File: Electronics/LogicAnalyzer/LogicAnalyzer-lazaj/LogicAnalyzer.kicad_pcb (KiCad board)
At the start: 4 copper layers, 57 x 55.2 mm, 58 parts, among them J1 Conn_02x15_Odd_Even, J2 Conn_01x03, J3 Conn_01x03, U1 Pico

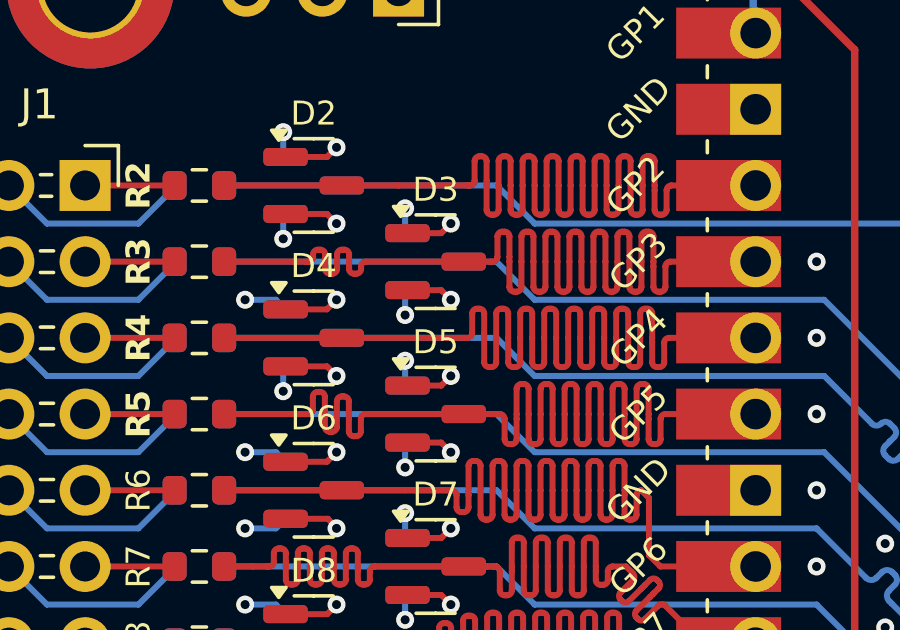
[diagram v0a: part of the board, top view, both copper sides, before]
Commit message: pcb: add track to avoid isolated copper fill island
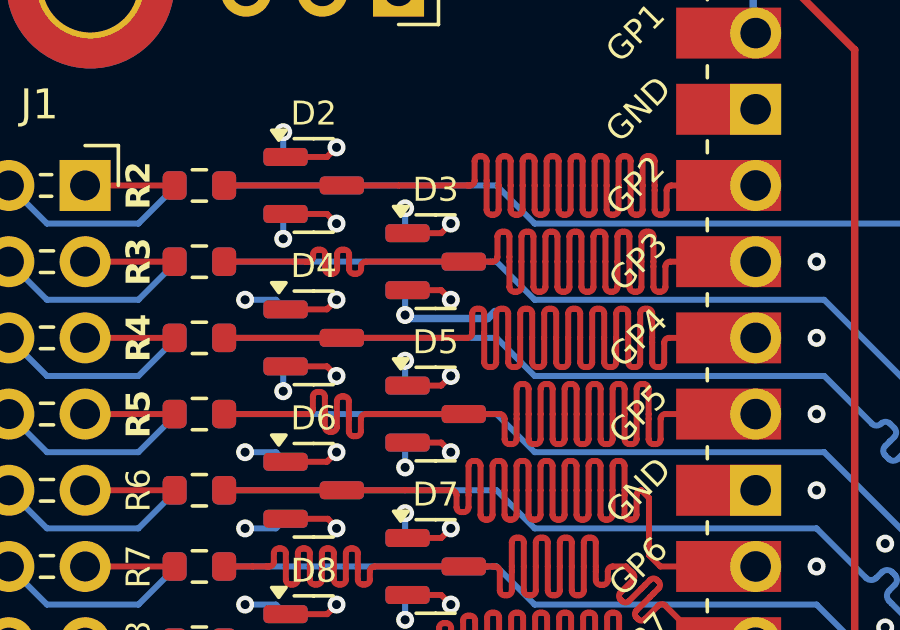
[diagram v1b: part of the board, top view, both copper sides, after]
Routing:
- net /GND: track 41.3 -> 44.4 mm
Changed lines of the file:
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@@
 		(tags "Through hole angled socket strip THT 1x03 2.54mm single row")
 		(property "Reference" "J2"
-			(at 2.157 2.65 360)
+			(at 2.157 2.65 0)
 			(layer "F.SilkS")
 			(hide yes)
@@
 	)
 	(segment
+		(start 89.408 80.518)
+		(end 89.525 80.635)
+		(width 0.25)
+		(layer "B.Cu")
+		(net 25)
+	)
+	(segment
+		(start 92.165 80.635)
+		(end 92.4 80.4)
+		(width 0.25)
+		(layer "B.Cu")
+		(net 25)
+	)
+	(segment
 		(start 85.344 82.3085)
 		(end 85.4225 82.23)
@@
 		(layer "B.Cu")
 		(net 25)
+	)
+	(segment
+		(start 89.525 80.635)
+		(end 92.165 80.635)
+		(width 0.25)
+		(layer "B.Cu")
+		(net 25)

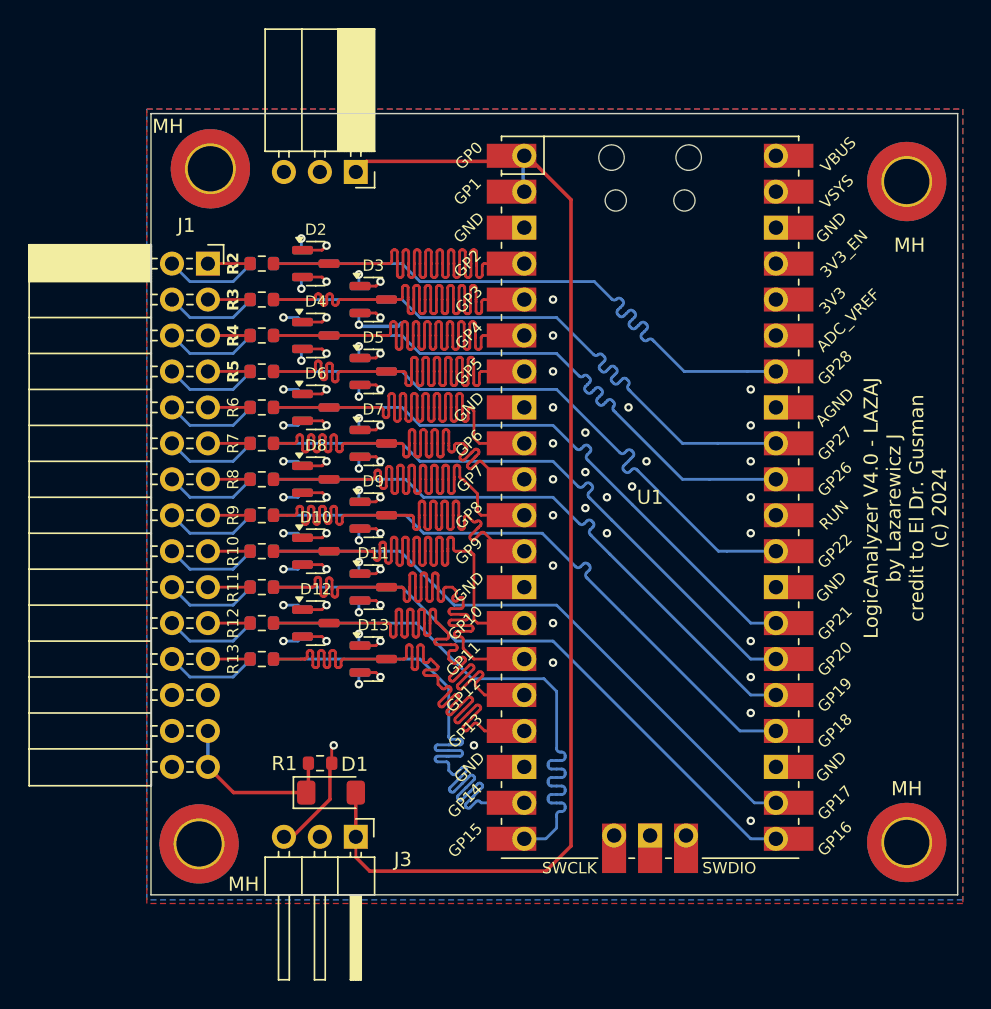
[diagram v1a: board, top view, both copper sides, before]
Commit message: sch and pcb: add mountingholes to schematic and pcb to have parity
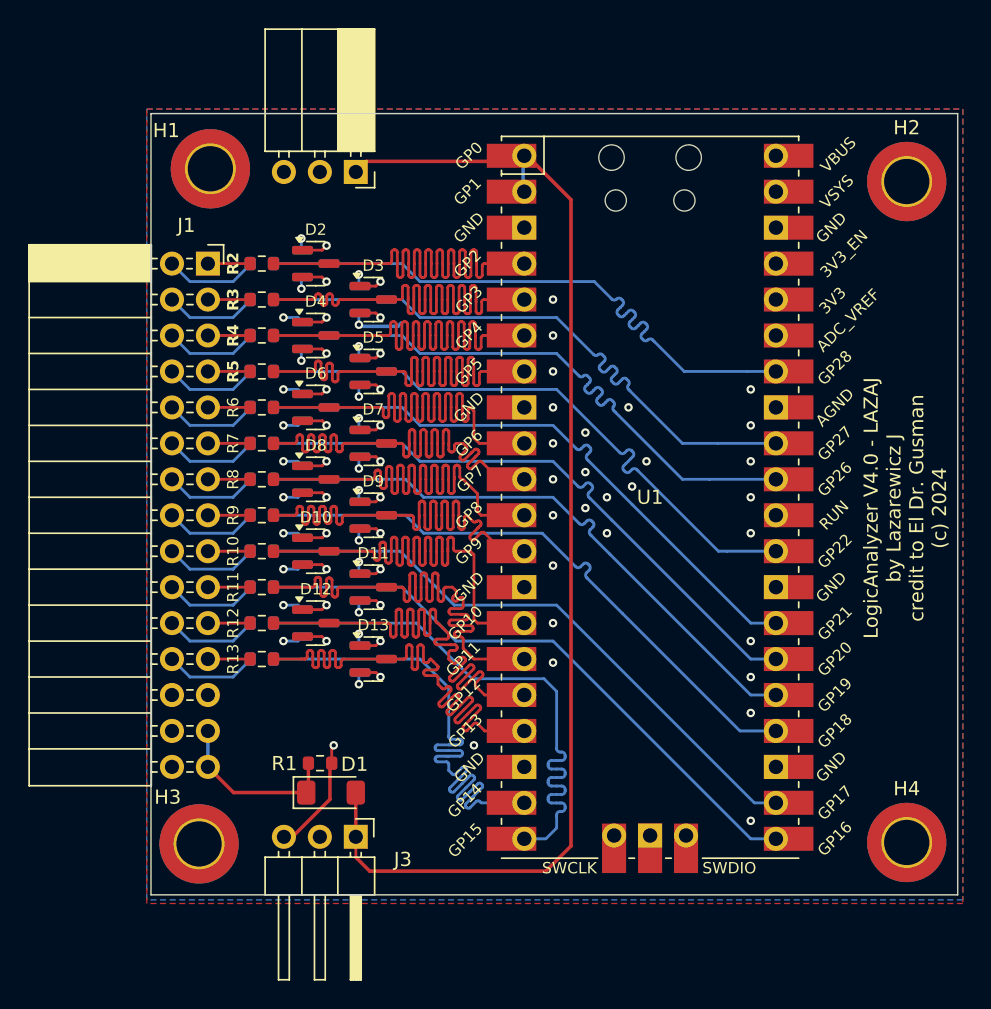
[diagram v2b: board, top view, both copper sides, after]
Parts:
- removed MH (x4): MountingHole_3.2mm_M3_DIN965_Pad_TopBottom, MountingHole:MountingHole_3.2mm_M3_DIN965_Pad_TopBottom
- added H1: MountingHole, MountingHole:MountingHole_3.2mm_M3_DIN965_Pad_TopBottom, F.Cu at (78.9, 69.5)
- added H2: MountingHole, MountingHole:MountingHole_3.2mm_M3_DIN965_Pad_TopBottom, F.Cu at (128.1, 70.4)
- added H3: MountingHole, MountingHole:MountingHole_3.2mm_M3_DIN965_Pad_TopBottom, F.Cu at (78.1, 117.2)
- added H4: MountingHole, MountingHole:MountingHole_3.2mm_M3_DIN965_Pad_TopBottom, F.Cu at (128.1, 117.1)

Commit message: add LCSC partnumbers, turn off refdes for mounting holes
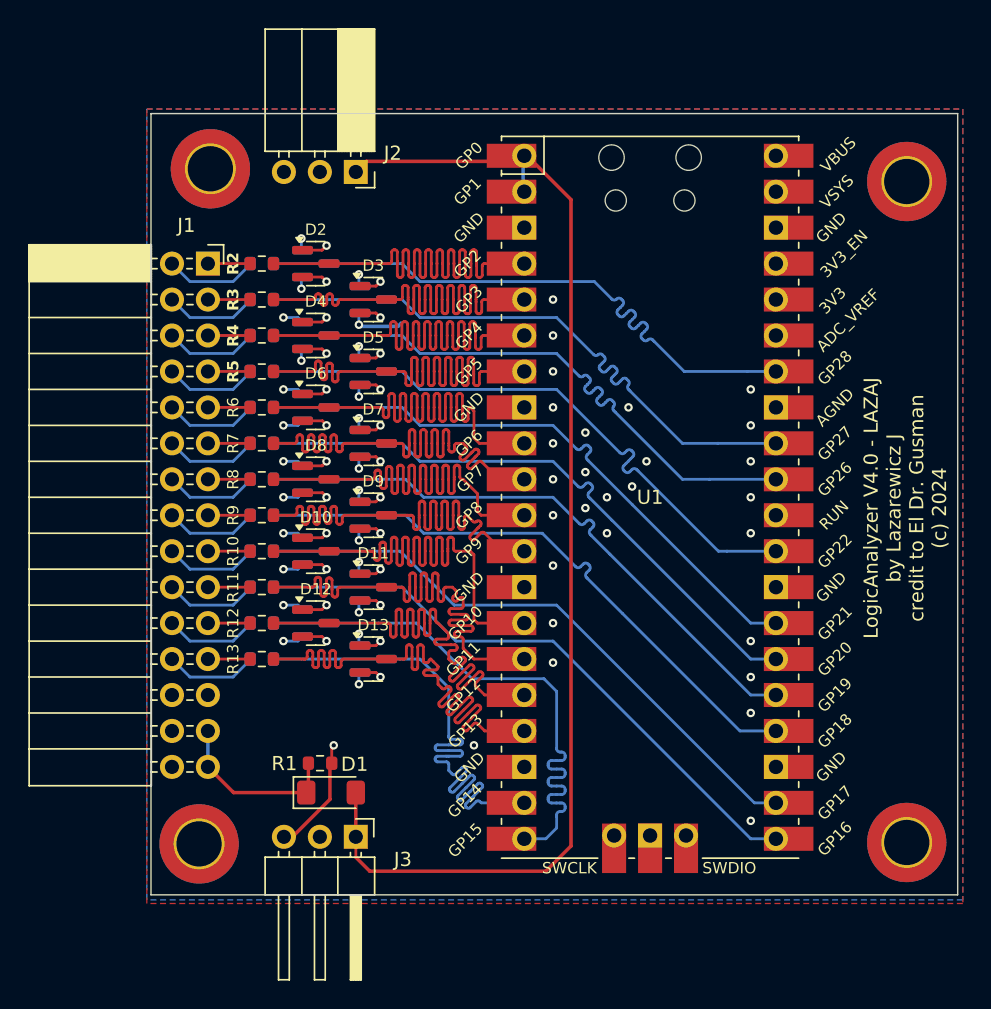
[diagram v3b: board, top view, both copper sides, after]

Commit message: mounting holes: change to a footprint that has no electrical connection, pcb: make sure mounting holes are aligned horizontally and vertically
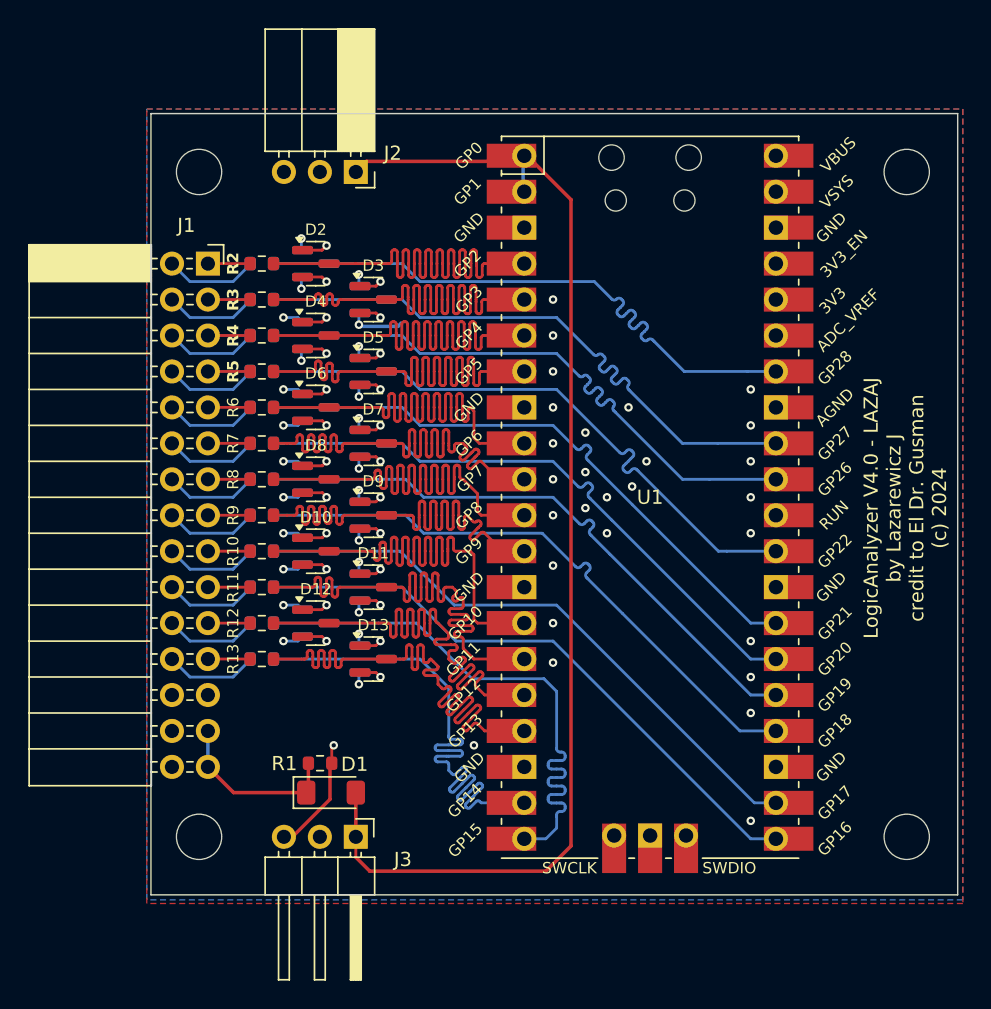
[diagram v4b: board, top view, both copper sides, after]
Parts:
- H1, H2, H3, H4: footprint MountingHole:MountingHole_3.2mm_M3_DIN965_Pad_TopBottom -> MountingHole:MountingHole_3.2mm_M3_DIN965
- moved H1 0.83 mm to (78.1, 69.7)
- moved H2 0.68 mm to (128.1, 69.7)
- moved H3 0.50 mm to (78.1, 116.7)
- moved H4 0.40 mm to (128.1, 116.7)
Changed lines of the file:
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@@
 		)
 	)
-	(footprint "MountingHole:MountingHole_3.2mm_M3_DIN965_Pad_TopBottom"
+	(footprint "MountingHole:MountingHole_3.2mm_M3_DIN965"
 		(layer "F.Cu")
-		(at 78.115 117.2)
-		(descr "Mounting Hole 3.2mm, M3, DIN965")
-		(tags "mounting hole 3.2mm m3 din965")
+		(at 78.115 116.7)
+		(descr "Mounting Hole 3.2mm, no annular, M3, DIN965")
+		(tags "mounting hole 3.2mm no annular m3 din965")
 		(property "Reference" "H3"
-			(at -2.215 -3.3 0)
+			(at 0 -3.8 0)
 			(layer "F.SilkS")
 			(hide yes)
@@
 			)
 		)
-		(property "Footprint" "MountingHole:MountingHole_3.2mm_M3_DIN965_Pad_TopBottom"
+		(property "Footprint" "MountingHole:MountingHole_3.2mm_M3_DIN965"
 			(at 0 0 0)
 			(unlocked yes)
@@
 			)
 		)
-		(pad "1" thru_hole circle
+		(pad "" np_thru_hole circle
 			(at 0 0)
-			(size 3.6 3.6)
+			(size 3.2 3.2)
 			(drill 3.2)
 			(layers "*.Cu" "*.Mask")
-			(remove_unused_layers no)
-		)
-		(pad "1" connect circle
-			(at 0 0)
-			(size 5.6 5.6)
-			(layers "F.Cu" "F.Mask")
-		)
-		(pad "1" connect circle
-			(at 0 0)
-			(size 5.6 5.6)
-			(layers "B.Cu" "B.Mask")
 		)
 	)
@@
 		(sheetname "Root")
 		(sheetfile "LogicAnalyzer.kicad_sch")
-		(attr through_hole)
+		(attr through_hole dnp)
 		(fp_line
 			(start -10.09 6.41)
@@
 		(sheetname "Root")
 		(sheetfile "LogicAnalyzer.kicad_sch")
-		(attr through_hole)
+		(attr through_hole dnp)
 		(fp_line
 			(start -10.5 -25.5)
@@
 		)
 	)
-	(footprint "MountingHole:MountingHole_3.2mm_M3_DIN965_Pad_TopBottom"
+	(footprint "MountingHole:MountingHole_3.2mm_M3_DIN965"
 		(layer "F.Cu")
-		(at 128.115 117.1)
-		(descr "Mounting Hole 3.2mm, M3, DIN965")
-		(tags "mounting hole 3.2mm m3 din965")
+		(at 128.115 116.7)
+		(descr "Mounting Hole 3.2mm, no annular, M3, DIN965")
+		(tags "mounting hole 3.2mm no annular m3 din965")
 		(property "Reference" "H4"
 			(at 0 -3.8 0)
@@
 			)
 		)
-		(property "Footprint" "MountingHole:MountingHole_3.2mm_M3_DIN965_Pad_TopBottom"
+		(property "Footprint" "MountingHole:MountingHole_3.2mm_M3_DIN965"
 			(at 0 0 0)
 			(unlocked yes)
@@
 			)
 		)
-		(pad "1" thru_hole circle
+		(pad "" np_thru_hole circle
 			(at 0 0)
-			(size 3.6 3.6)
+			(size 3.2 3.2)
 			(drill 3.2)
 			(layers "*.Cu" "*.Mask")
-			(remove_unused_layers no)
-		)
-		(pad "1" connect circle
-			(at 0 0)
-			(size 5.6 5.6)
-			(layers "F.Cu" "F.Mask")
-		)
-		(pad "1" connect circle
-			(at 0 0)
-			(size 5.6 5.6)
-			(layers "B.Cu" "B.Mask")
 		)
 	)
@@
 		(sheetname "Root")
 		(sheetfile "LogicAnalyzer.kicad_sch")
-		(attr through_hole)
+		(attr through_hole dnp)
 		(fp_line
 			(start 1.44 6.41)
@@
 		)
 	)
-	(footprint "MountingHole:MountingHole_3.2mm_M3_DIN965_Pad_TopBottom"
+	(footprint "MountingHole:MountingHole_3.2mm_M3_DIN965"
 		(layer "F.Cu")
-		(at 78.915 69.5)
-		(descr "Mounting Hole 3.2mm, M3, DIN965")
-		(tags "mounting hole 3.2mm m3 din965")
+		(at 78.115 69.725)
+		(descr "Mounting Hole 3.2mm, no annular, M3, DIN965")
+		(tags "mounting hole 3.2mm no annular m3 din965")
 		(property "Reference" "H1"
-			(at -3.115 -2.7 0)
+			(at 0 -3.8 0)
 			(layer "F.SilkS")
 			(hide yes)
@@
 			)
 		)
-		(property "Footprint" "MountingHole:MountingHole_3.2mm_M3_DIN965_Pad_TopBottom"
+		(property "Footprint" "MountingHole:MountingHole_3.2mm_M3_DIN965"
 			(at 0 0 0)
 			(unlocked yes)
@@
 			)
 		)
-		(pad "1" thru_hole circle
+		(pad "" np_thru_hole circle
 			(at 0 0)
-			(size 3.6 3.6)
+			(size 3.2 3.2)
 			(drill 3.2)
 			(layers "*.Cu" "*.Mask")
-			(remove_unused_layers no)
-		)
-		(pad "1" connect circle
-			(at 0 0)
-			(size 5.6 5.6)
-			(layers "F.Cu" "F.Mask")
-		)
-		(pad "1" connect circle
-			(at 0 0)
-			(size 5.6 5.6)
-			(layers "B.Cu" "B.Mask")
 		)
 	)
@@
 		)
 	)
-	(footprint "MountingHole:MountingHole_3.2mm_M3_DIN965_Pad_TopBottom"
+	(footprint "MountingHole:MountingHole_3.2mm_M3_DIN965"
 		(layer "F.Cu")
-		(at 128.115 70.4)
-		(descr "Mounting Hole 3.2mm, M3, DIN965")
-		(tags "mounting hole 3.2mm m3 din965")
+		(at 128.115 69.725)
+		(descr "Mounting Hole 3.2mm, no annular, M3, DIN965")
+		(tags "mounting hole 3.2mm no annular m3 din965")
 		(property "Reference" "H2"
 			(at 0 -3.8 0)
@@
 			)
 		)
-		(property "Footprint" "MountingHole:MountingHole_3.2mm_M3_DIN965_Pad_TopBottom"
+		(property "Footprint" "MountingHole:MountingHole_3.2mm_M3_DIN965"
 			(at 0 0 0)
 			(unlocked yes)
@@
 			)
 		)
-		(pad "1" thru_hole circle
+		(pad "" np_thru_hole circle
 			(at 0 0)
-			(size 3.6 3.6)
+			(size 3.2 3.2)
 			(drill 3.2)
 			(layers "*.Cu" "*.Mask")
-			(remove_unused_layers no)
-		)
-		(pad "1" connect circle
-			(at 0 0)
-			(size 5.6 5.6)
-			(layers "F.Cu" "F.Mask")
-		)
-		(pad "1" connect circle
-			(at 0 0)
-			(size 5.6 5.6)
-			(layers "B.Cu" "B.Mask")
 		)
 	)
@@
 		(sheetname "Root")
 		(sheetfile "LogicAnalyzer.kicad_sch")
-		(attr through_hole)
+		(attr through_hole dnp)
 		(fp_line
 			(start -12.63 -1.33)
